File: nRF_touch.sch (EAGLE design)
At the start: 46 parts, among them Q1 BSS138BKW, T1 BSS84, T2 BC847/2N7002, U1 ADP160, U2 AT42QT1010-TSHR

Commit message: Start placing components
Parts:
- removed J2: (no value), SparkFun-Connectors:CONN_09
- removed J3: (no value), SparkFun-Connectors:CONN_03
- removed R3, R4: 4.7k, SparkFun-Resistors:4.7KOHM-0603-1/10W-1%
- removed U$1: N5150, N5:N5150
- added C12: 4.7uF, SparkFun-Capacitors:0.1UF-0603-25V-(+80/-20%)
- added C13, C14: 0.1uF, SparkFun-Capacitors:0.1UF-0603-25V-(+80/-20%)
- added C15: 1uF, SparkFun-Capacitors:4.7UF0603
- added C16, C18, C19: 0.1uF, SparkFun-Capacitors:4.7UF0603
- added C17: 4.7uF, SparkFun-Capacitors:4.7UF0603
- added C20, C21, C22, C23: 12pF, SparkFun-Capacitors:4.7UF0603
- added C24: 100pF, SparkFun-Capacitors:4.7UF0603
- added C25: 0.8pF, SparkFun-Capacitors:4.7UF0603
- added C26: DNP, SparkFun-Capacitors:4.7UF0603
- added D2: BAT54C, nxp_60:BAT754C
- added D3: BAT754A, nxp_60:BAT754A
- added E1: ANTENNA-GROUNDEDTRACE-15.2MM, SparkFun-RF:ANTENNA-GROUNDEDTRACE-15.2MM
- added FB1: FB_0805, ferrite_beads:FB_0805
- added FB2: 3.9nH, ferrite_beads:FB_0805
- added IC1: MCP73831/OT, adafruit:MCP73831/OT
- added J1, J4, J5, J6, J7: (no value), SparkFun-Connectors:CONN_02
- added MBAT, SWDCLK, SWDIO, VBAT: TESTPOINT, test_points:TESTPOINT
- added R16, R17: 10k, SparkFun-Resistors:4.7KOHM-0603-1/10W-1%
- added R18: 2k, SparkFun-Resistors:4.7KOHM-0603-1/10W-1%
- added R19: 0.010, SparkFun-Resistors:4.7KOHM-0603-1/10W-1%
- added U$6: NRF52832NRF52832-QFAA, NRF52832:NRF52832NRF52832-QFAA
- added Y1: 32.768kHz, SparkFun-Clocks:CRYSTAL-32.768KHZSMD-3.2X1.5
- added Y2: 32MHz-3.2X2.5, SparkFun-Clocks:CRYSTAL-GROUNDEDSMD-5X3.2
- C2, C4: value 0.1uF -> 22nF
- C3, C6, C8: device SparkFun-Capacitors:0.1UF-0603-25V-5% -> SparkFun-Capacitors:0.1UF-0603-25V-(+80/-20%)
- C5: value 1uF -> 220nF; device SparkFun-Capacitors:0.1UF-0603-25V-5% -> SparkFun-Capacitors:0.1UF-0603-25V-(+80/-20%)
- R1: value 4.7k -> 200k
- R2: value 4.7k -> 1k
- U$3: value FLASH -> STC3100; device FlashMem:FLASH -> STC3100:STC3100
- U2: value AT42QT1010-TSHR -> AT42QT1040; device AT42QT1010:AT42QT1010-TSHR -> AT42QT1040:AT42QT1040
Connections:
- removed net 5V: C10.2, C8.1, J2.1, R8.2, T1.S, U1.VIN, U2.VDD
- removed net AIN3: S3.P$1, U$1.P002/AIN3
- removed net AIN5: S1.P$1, U$1.P004/AIN5
- removed net AT42_OUT: D1.A2, U2.OUT
- removed net N$1: R12.2, U$1.P024
- removed net PAD: R11.1, S2.P$1
- removed net SPIS_MI: J2.5
- removed net SPIS_MO: J2.6
- removed net SPIS_SCK: J2.4
- removed net SST_CS: J2.7, U$3.CE
- new net AT42_COUT: D1.A2, U$6.P18, U2.OUT2
- new net AT42_DOUT: U$6.P17, U2.OUT3
- new net AT42_GOUT: U$6.P19, U2.OUT0
- new net CHRG_END: IC1.STAT, U$6.P20
- new net CPAD: R17.1, S2.P$1
- new net DPAD: R16.1, S1.P$1
- new net GPAD: R11.1, S3.P$1
- new net LED_PIN: R12.2, U$6.P14
- new net MBAT: MBAT.P$1, R19.1, U$3.CG
- new net N$14: IC1.PROG, R18.2
- new net N$16: R1.1, U$3.ROSC
- new net N$17: C15.1, FB1.2, U$6.DEC4
- new net N$18: C25.1, FB2.2, U$6.ANT
- new net N$19: FB1.1, U$6.DCC
- new net N$20: C16.1, U$6.DEC1
- new net N$21: C26.1, E1.SIGNAL, FB2.1
- new net N$24: C20.2, U$6.P0/XL1, Y1.2
- new net N$25: C21.2, U$6.P1/XL2, Y1.1
- new net N$27: C22.1, U$6.XC2, Y2.2
- new net N$28: C23.1, U$6.XC1, Y2.1
- new net N$3: C2.2, R16.2, U2.SNSK3
- new net N$4: C2.1, U2.SNS3
- new net N$5: C4.2, R17.2, U2.SNSK2
- new net N$9: C4.1, U2.SNS2
- new net SELF_EN: D2.A2, U$6.P15
- new net VBAT: C10.2, C8.1, IC1.VBAT, R8.2, T1.S, U1.VIN, U2.VDD, VBAT.P$1
- new net VUSB: C6.1, D2.A1, IC1.VDD, J4.2
- net 5150_CS: now also J4.1, U$6.P28/AIN4; no longer J2.3, U$1.P015
- net GND: now also C12.1, C13.1, C14.1, C15.2, C16.2, C17.1, C18.2, C19.2, C20.1, C21.1, C22.2, C23.2, C24.2, C25.2, C26.2, C5.1, E1.GND, IC1.VSS, J1.1, R1.2, R18.1, R19.2, U$3.GND, U$6.VSS, U$6.VSS2, Y2.3; no longer C2.2, C4.2, C5.2, J2.2, U$1.GND, U$3.VSS, U2.SYNC/MODE
- net N$12: now also C5.2, R2.1, U$3.VIN; no longer R1.2, U$3.WP
- net N$15: now also C24.1, U$6.DEC3; no longer R2.1, U$3.HOLD
- net N$6: now also U2.SNSK0; no longer U2.SNSK
- net N$7: now also U2.SNS0; no longer U2.SNS
- net NEO_PIN: now also U$6.P16; no longer U$1.P008
- net NRF_EN: now also D2.K1K2; no longer U$1.P021
- net SCL: now also J7.2, U$3.SCL; no longer R4.2, U$1.P031
- net SDA: now also J7.1, U$3.SDA; no longer R3.1, U$1.P030
- net SHARP_CS: now also J5.2, U$6.P29/AIN5
- net SPIM_DIN: now also J6.2, U$6.P26; no longer U$1.P011, U$3.SO
- net SPIM_DO: now also J5.1, U$6.P27; no longer U$1.P012, U$3.SI
- net SPIM_SCK: now also J6.1, U$6.P25; no longer U$1.P009, U$3.SCK
- net SWDCLK: now also SWDCLK.P$1, U$6.CLK; no longer J3.2, U$1.SWDCLK
- net SWDIO: now also SWDIO.P$1, U$6.DIO; no longer J3.1, U$1.SWDIO
- net SW_POWER: now also C3.1, R2.2, U$3.VCC
- net VCC: now also C12.2, C13.2, C14.2, C17.2, C18.1, C19.1, J1.2, U$6.VDD, U$6.VDD2, U$6.VDD3; no longer C2.1, C3.1, C4.1, C5.1, C6.1, J2.9, J3.3, R1.1, R2.2, R3.2, R4.1, U$1.VCC, U$3.VDD

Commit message: Finished placing
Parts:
- removed D1: BAT54C, nxp_60:BAT754C
- added C27, C28: 4.7uF, SparkFun-Capacitors:0.1UF-0603-25V-(+80/-20%)
- added C29: 0.1uF, SparkFun-Capacitors:0.1UF-0603-25V-(+80/-20%)
- added R3: 47, SparkFun-Resistors:4.7KOHM-0603-1/10W-1%
- added R4: 80, SparkFun-Resistors:4.7KOHM-0603-1/10W-1%
- added T3, T4: BC847, nxp_60:BC847
- added U$1, U$7, U$8: KPA-2106SECK, KPA_LED:KPA-2106SECK
- D3: value BAT754A -> BAT54A
- MBAT, SWDCLK, SWDIO, VBAT: value TESTPOINT -> TESTPOINT_22; device test_points:TESTPOINT -> test_points:TESTPOINT_22
- T2: value BC847/2N7002 -> BC847
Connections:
- removed net NRF_EN: D1.A1, D2.K1K2
- new net LED_BCK: T3.B, T4.B, U$6.P13
- new net N$1: R9.2, T2.B
- new net N$10: R3.2, U$1.P$2, U$7.P$2
- new net N$22: T4.C, U$8.P$1
- new net SW_AT: C9.1, D2.A2, L1.VDD, R13.2, R14.2, T1.D
- new net TRANS: D3.K1, T2.C
- net AT42_COUT: now also D3.K2, U2.OUT1; no longer D1.A2, U2.OUT2
- net CHRG_END: now also U$6.P31/AIN7; no longer U$6.P20
- net GND: now also C27.1, C28.1, C29.1, T3.E, T4.E
- net N$11: now also R4.2, U$8.P$2; no longer C11.1, R9.2, T2.B
- net N$13: now also T3.C, U$1.P$1, U$7.P$1; no longer D1.K1K2, R10.1, R9.1
- net N$5: now also U2.SNSK1; no longer U2.SNSK2
- net N$8: now also C11.1, D3.A1A2; no longer T2.C
- net N$9: now also U2.SNS1; no longer U2.SNS2
- net SCL: now also U$6.P20
- net SDA: now also U$6.P15
- net SELF_EN: now also R10.1, R9.1, U$6.P30/AIN6; no longer D2.A2, U$6.P15
- net SW_POWER: now also D2.K1K2; no longer C9.1, L1.VDD, R13.2, R14.2, T1.D
- net VBAT: now also C28.2
- net VCC: now also C27.2, C29.2, R3.1, R4.1
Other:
- moved on the sheet: C11, C3, C4, C5, C9, D2, D3, LED1, R1, R10, R12, R13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

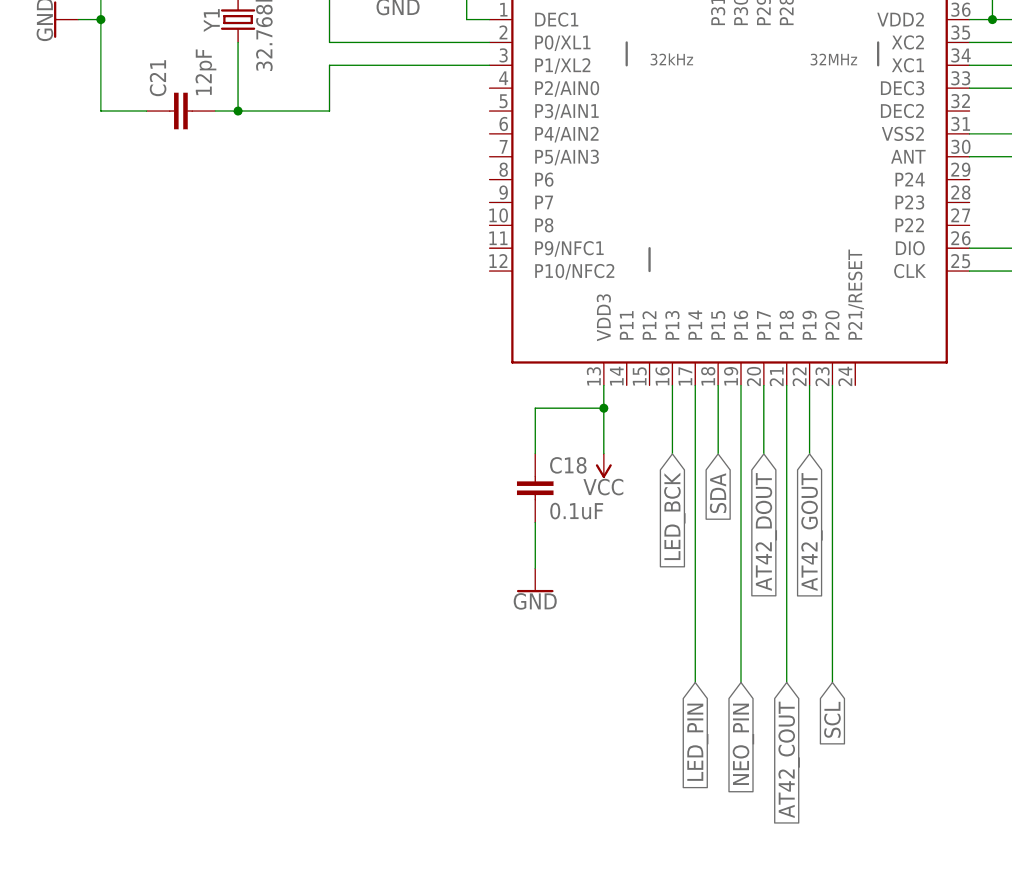
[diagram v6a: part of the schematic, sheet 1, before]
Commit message: First try at routing
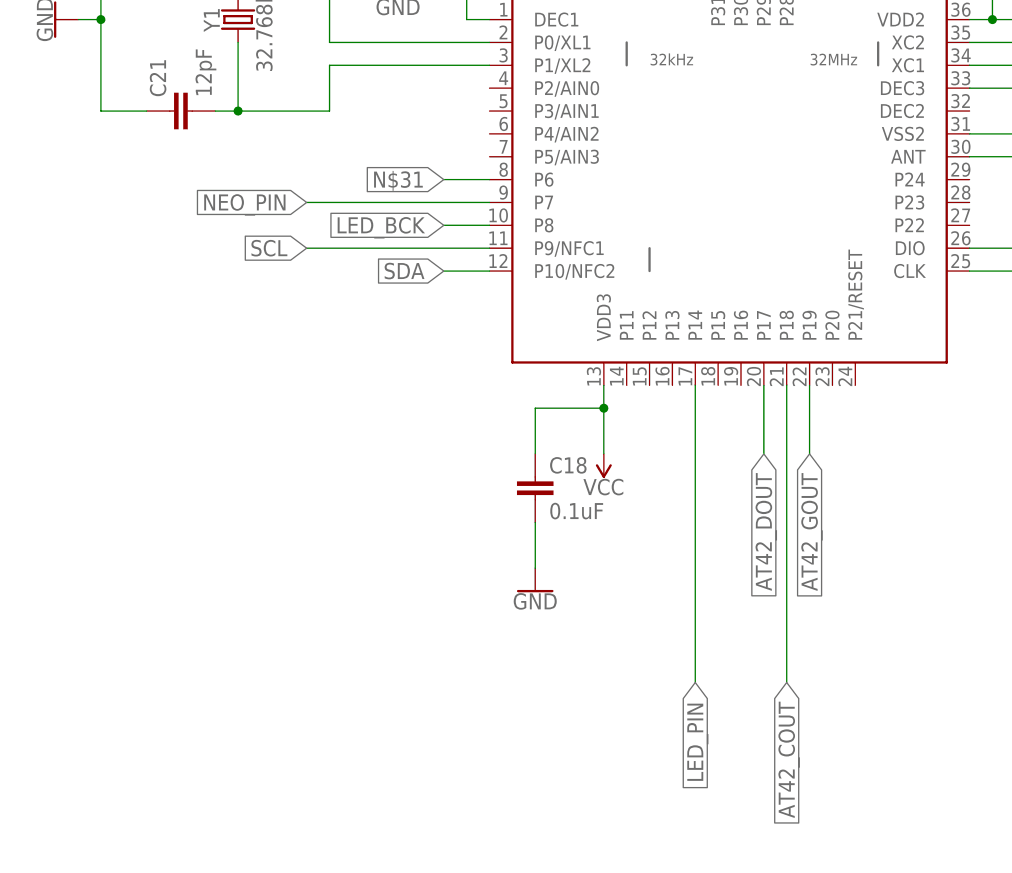
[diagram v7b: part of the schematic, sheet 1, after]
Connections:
- new net N$31: U$6.P6
- net LED_BCK: now also U$6.P8; no longer U$6.P13
- net NEO_PIN: now also U$6.P7; no longer U$6.P16
- net SCL: now also U$6.P9/NFC1; no longer U$6.P20
- net SDA: now also U$6.P10/NFC2; no longer U$6.P15
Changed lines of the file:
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@@
 </segment>
 <segment>
-<pinref part="U$6" gate="G$1" pin="P20"/>
-<wire x1="-40.64" y1="-53.34" x2="-40.64" y2="-86.36" width="0.1524" layer="91"/>
-<label x="-40.64" y="-86.36" size="1.778" layer="95" rot="R270" xref="yes"/>
+<pinref part="U$6" gate="G$1" pin="P9/NFC1"/>
+<wire x1="-78.74" y1="-38.1" x2="-99.06" y2="-38.1" width="0.1524" layer="91"/>
+<label x="-99.06" y="-38.1" size="1.778" layer="95" rot="R180" xref="yes"/>
 </segment>
 </net>
@@
 </segment>
 <segment>
-<pinref part="U$6" gate="G$1" pin="P15"/>
-<wire x1="-53.34" y1="-53.34" x2="-53.34" y2="-60.96" width="0.1524" layer="91"/>
-<label x="-53.34" y="-60.96" size="1.778" layer="95" rot="R270" xref="yes"/>
+<pinref part="U$6" gate="G$1" pin="P10/NFC2"/>
+<wire x1="-78.74" y1="-40.64" x2="-83.82" y2="-40.64" width="0.1524" layer="91"/>
+<label x="-83.82" y="-40.64" size="1.778" layer="95" rot="R180" xref="yes"/>
 </segment>
 </net>
@@
 <net name="NEO_PIN" class="0">
 <segment>
-<pinref part="U$6" gate="G$1" pin="P16"/>
-<wire x1="-50.8" y1="-53.34" x2="-50.8" y2="-86.36" width="0.1524" layer="91"/>
-<label x="-50.8" y="-86.36" size="1.778" layer="95" rot="R270" xref="yes"/>
+<pinref part="U$6" gate="G$1" pin="P7"/>
+<wire x1="-78.74" y1="-33.02" x2="-99.06" y2="-33.02" width="0.1524" layer="91"/>
+<label x="-99.06" y="-33.02" size="1.778" layer="95" rot="R180" xref="yes"/>
 </segment>
 </net>
@@
 <net name="LED_BCK" class="0">
 <segment>
-<pinref part="U$6" gate="G$1" pin="P13"/>
-<wire x1="-58.42" y1="-53.34" x2="-58.42" y2="-60.96" width="0.1524" layer="91"/>
-<label x="-58.42" y="-60.96" size="1.778" layer="95" rot="R270" xref="yes"/>
-</segment>
-</net>
+<pinref part="U$6" gate="G$1" pin="P8"/>
+<wire x1="-78.74" y1="-35.56" x2="-83.82" y2="-35.56" width="0.1524" layer="91"/>
+<label x="-83.82" y="-35.56" size="1.778" layer="95" rot="R180" xref="yes"/>
+</segment>
+</net>
+<net name="N$31" class="0">
+<segment>
+<pinref part="U$6" gate="G$1" pin="P6"/>
+<wire x1="-78.74" y1="-30.48" x2="-83.82" y2="-30.48" width="0.1524" layer="91"/>
+<label x="-83.82" y="-30.48" size="1.778" layer="95" rot="R180" xref="yes"/>
+</segment>
+</net>

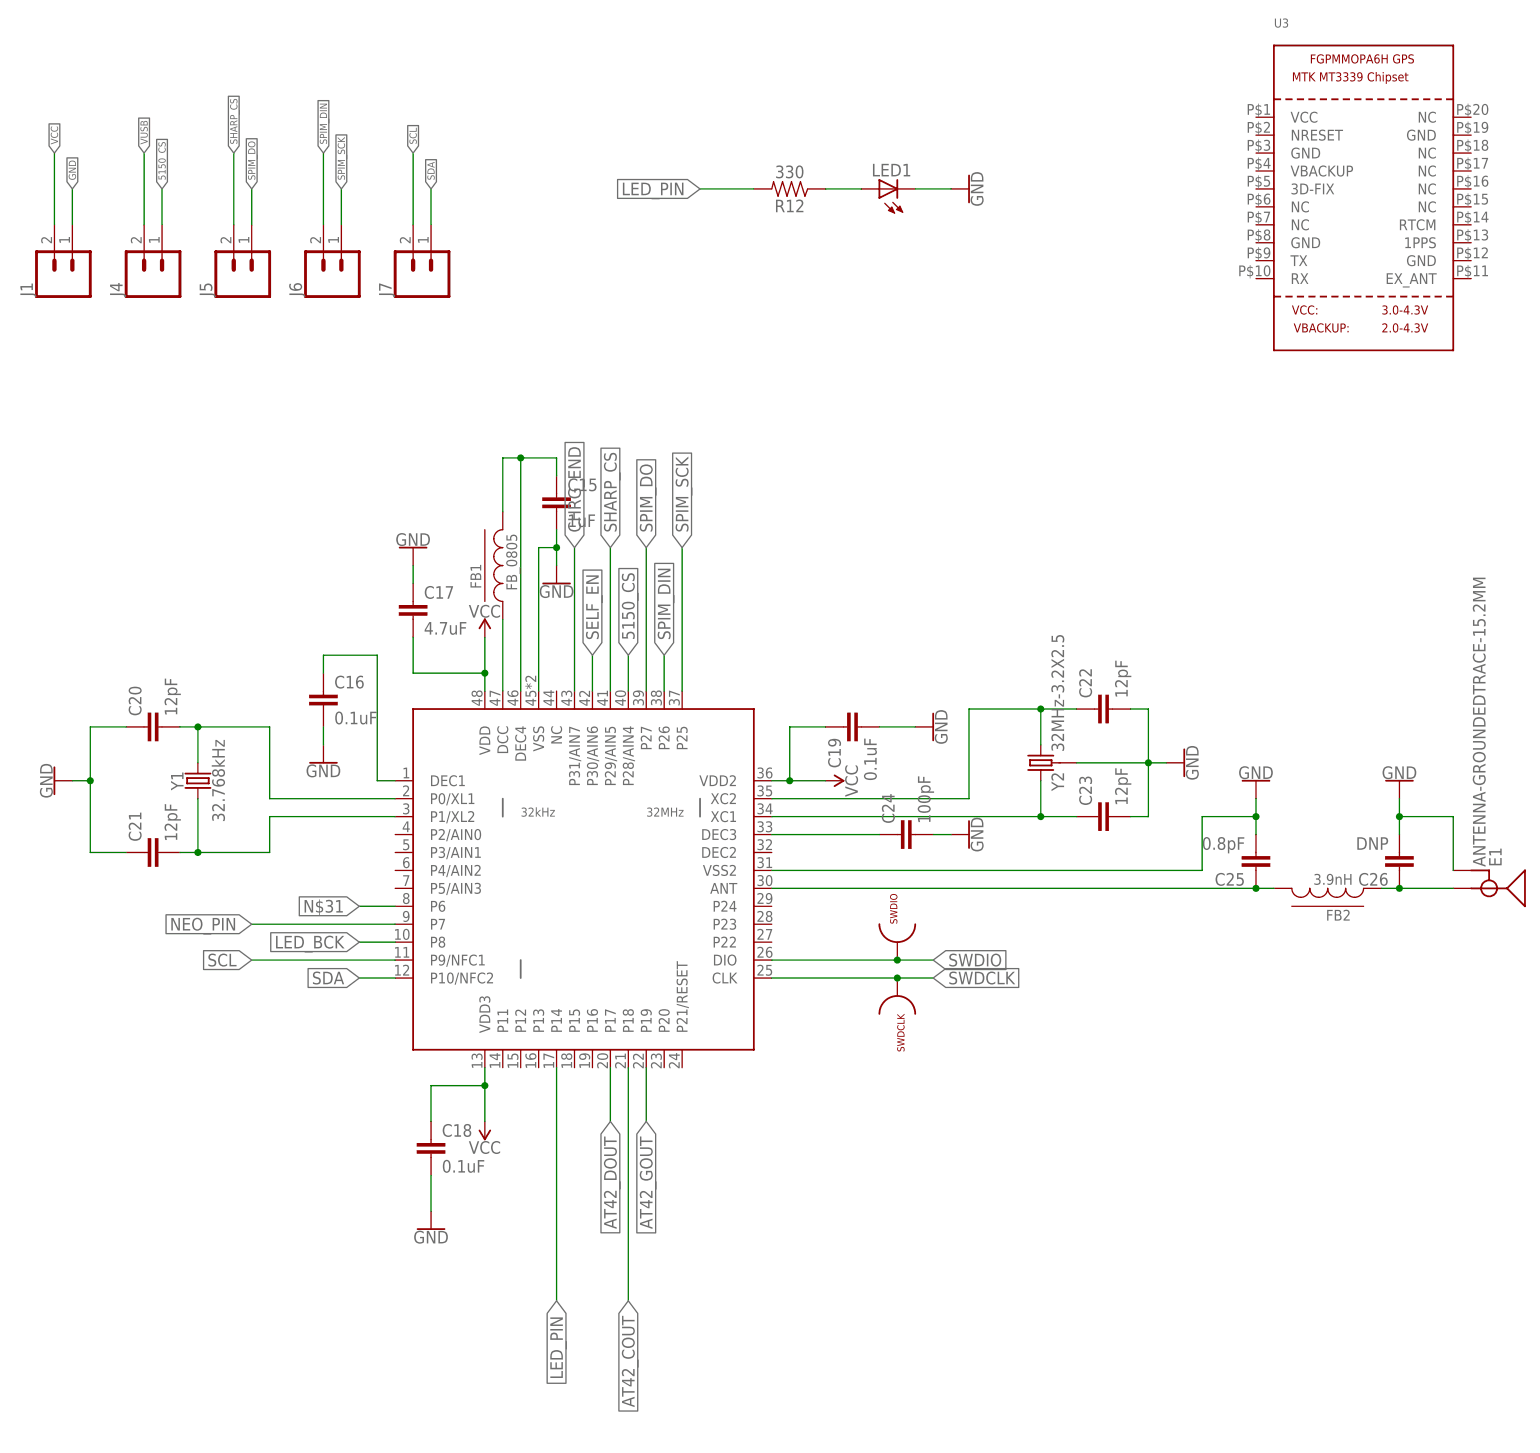
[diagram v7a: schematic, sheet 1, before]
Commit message: Added resistors Routing optimized
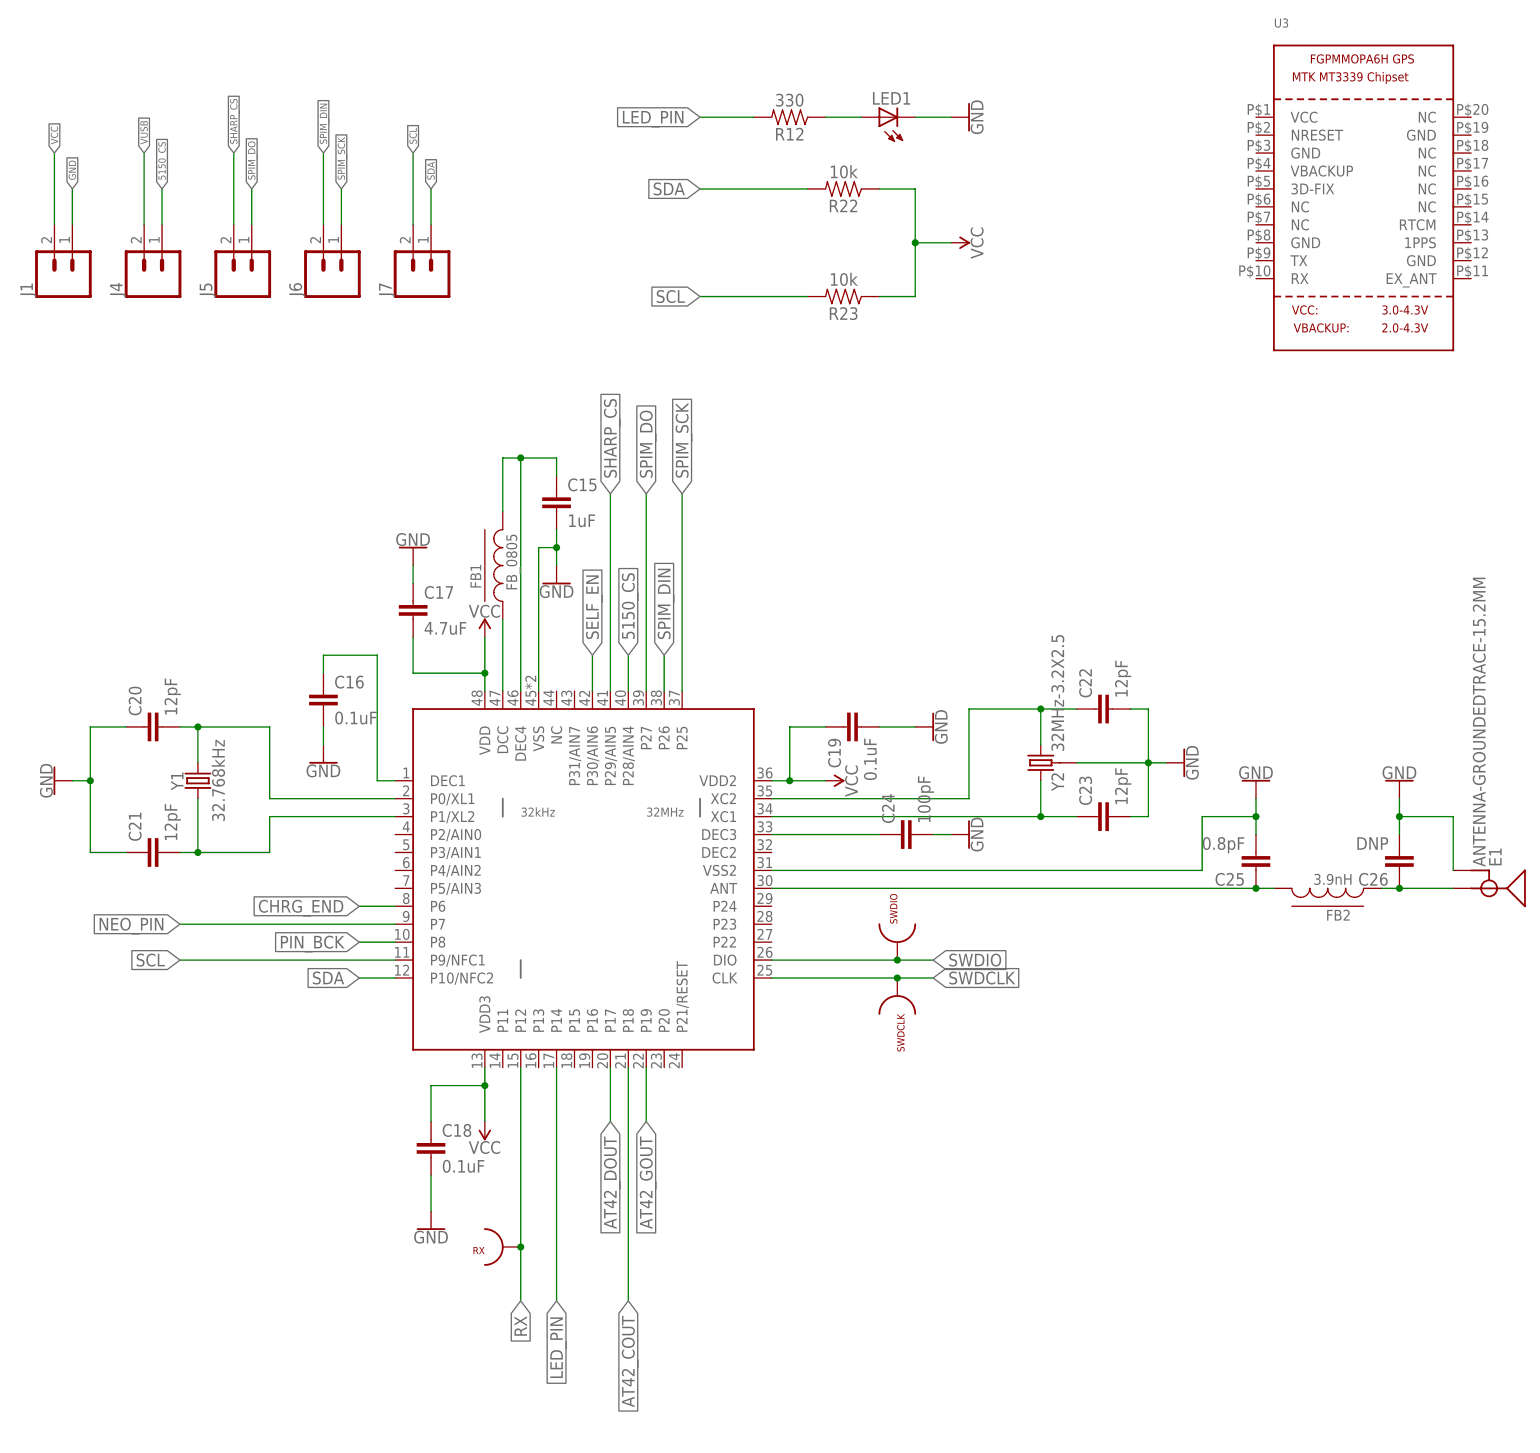
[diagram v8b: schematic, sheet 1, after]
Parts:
- added R20: 47k, SparkFun-Resistors:4.7KOHM-0603-1/10W-1%
- added R21: 100k, SparkFun-Resistors:4.7KOHM-0603-1/10W-1%
- added R22, R23: 10k, SparkFun-Resistors:4.7KOHM-0603-1/10W-1%
- added RX: TESTPOINT_22, test_points:TESTPOINT_22
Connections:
- removed net N$10: R3.2, U$1.P$2, U$7.P$2
- removed net N$31: U$6.P6
- new net N$23: R3.2, T3.C
- new net PIN_BCK: R21.1, U$6.P8
- new net RX: RX.P$1, U$6.P12
- net CHRG_END: now also U$6.P6; no longer U$6.P31/AIN7
- net GND: now also R20.2
- net LED_BCK: now also R21.2; no longer U$6.P8
- net N$13: now also R3.1; no longer T3.C
- net SCL: now also R23.2
- net SDA: now also R22.2
- net SW_POWER: now also R20.1
- net VCC: now also R22.1, R23.1, U$1.P$2, U$7.P$2; no longer R3.1
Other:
- moved on the sheet: LED1, MBAT, R12, R3, VBAT
